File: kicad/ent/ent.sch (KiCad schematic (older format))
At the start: 28 parts, among them J1 Conn_01x04_Male, J2 Conn_01x03_Male, J3 Conn_01x03_Male, J4 Conn_01x12_Male, J5 Conn_01x04_Male, J6 Conn_01x03_Male, J7 Conn_01x03_Male, SW1 SW_SPDT, SW2 SW_Push, U1 TPS62172DSG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

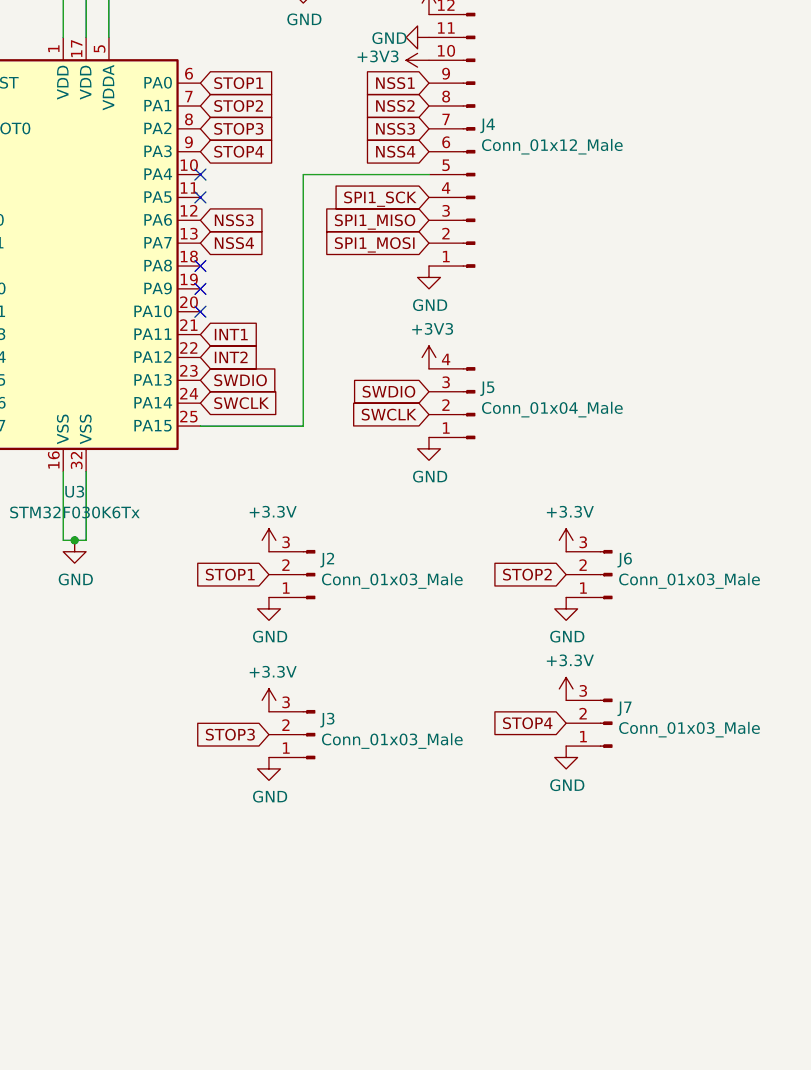
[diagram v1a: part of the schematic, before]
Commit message: added interface buttons
enkel schema
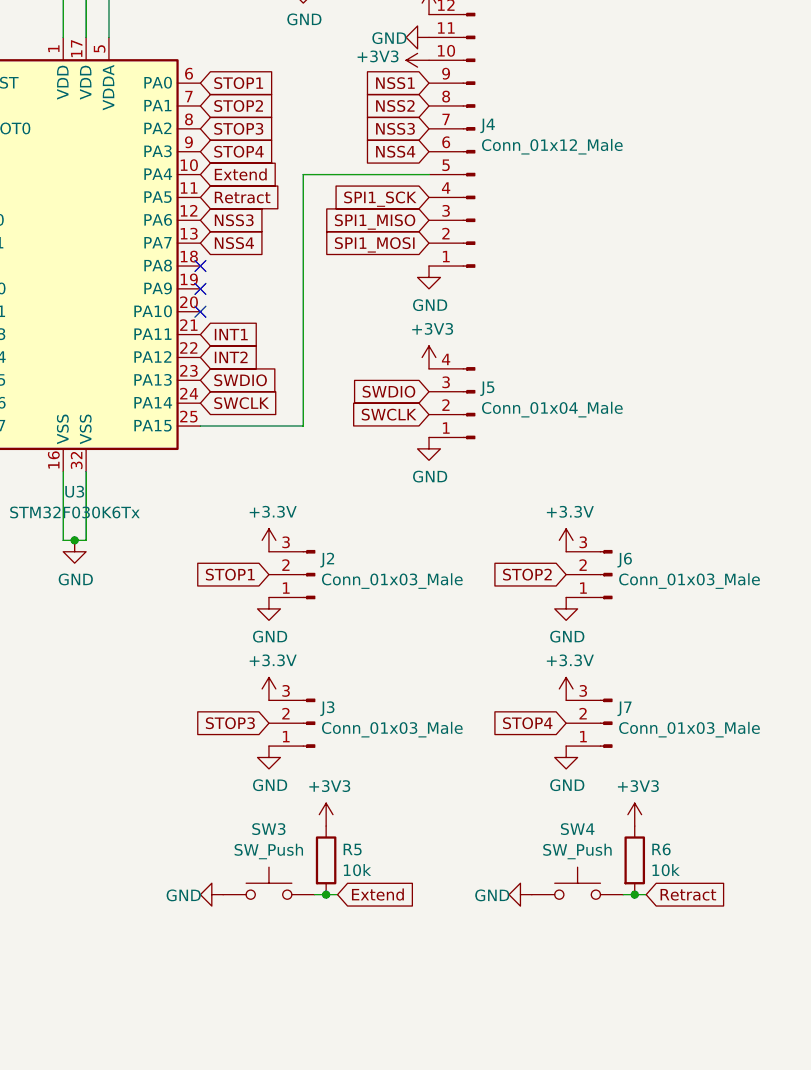
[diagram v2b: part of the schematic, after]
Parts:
- added R5, R6: 10k, Resistor_SMD:R_0805_2012Metric_Pad1.15x1.40mm_HandSolder, symbol Device:R
- added SW3, SW4: SW_Push, Button_Switch_SMD:SW_SPST_PTS645, symbol Switch:SW_Push
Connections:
- net +3V3: now also R5.1, R6.1
- net GND: now also SW3.1, SW4.1
- net Extend: now reaches U3.10 (PA4)
- net Extend: now also R5.2, SW3.2
- net Retract: now reaches U3.11 (PA5)
- net Retract: now also R6.2, SW4.2
- no-connect marks 7 -> 5
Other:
- moved on the sheet: J3
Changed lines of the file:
@@
 NoConn ~ 6700 2900
-$Comp
-L Switch:SW_Push SW2
-U 1 1 5E5EBC4B
-P 6300 2200
-F 0 "SW2" H 6300 2485 50  0000 C CNN
-F 1 "SW_Push" H 6300 2394 50  0000 C CNN
-F 2 "Button_Switch_SMD:SW_SPST_PTS645" H 6300 2400 50  0001 C CNN
-F 3 "~" H 6300 2400 50  0001 C CNN
-	1    6300 2200
-	1    0    0    -1
-$EndComp
-$Comp
-L power:GND #PWR014
-U 1 1 5E5EC8E1
-P 6100 2200
-F 0 "#PWR014" H 6100 1950 50  0001 C CNN
-F 1 "GND" V 6105 2027 50  0000 C CNN
-F 2 "" H 6100 2200 50  0001 C CNN
-F 3 "" H 6100 2200 50  0001 C CNN
-	1    6100 2200
-	0    1    1    0
-$EndComp
-Wire Wire Line
-	6500 2200 6600 2200
 $Comp
 L Device:C C5
@@
 	0    -1   -1   0
 $EndComp
-Wire Wire Line
-	6450 1800 6600 1800
-Wire Wire Line
-	6600 1800 6600 2200
-Connection ~ 6600 2200
-Wire Wire Line
-	6600 2200 6700 2200
 $Comp
 L power:GND #PWR015
@@
 Wire Wire Line
 	8250 2600 8800 2600
-NoConn ~ 7800 2600
-NoConn ~ 7800 2700
 Text GLabel 7800 2200 2    50   Input ~ 0
 STOP1
@@
 	1    0    0    -1
 $EndComp
-Text GLabel 8100 5050 0    50   Input ~ 0
+Text GLabel 8100 5000 0    50   Input ~ 0
 STOP3
 $Comp
 L Connector:Conn_01x03_Male J3
 U 1 1 5E66EF9D
-P 8300 5050
-F 0 "J3" H 8272 4982 50  0000 R CNN
-F 1 "Conn_01x03_Male" H 8272 5073 50  0000 R CNN
-F 2 "Connector_JST:JST_XH_B3B-XH-A_1x03_P2.50mm_Vertical" H 8300 5050 50  0001 C CNN
-F 3 "~" H 8300 5050 50  0001 C CNN
-	1    8300 5050
+P 8300 5000
+F 0 "J3" H 8272 4932 50  0000 R CNN
+F 1 "Conn_01x03_Male" H 8272 5023 50  0000 R CNN
+F 2 "Connector_JST:JST_XH_B3B-XH-A_1x03_P2.50mm_Vertical" H 8300 5000 50  0001 C CNN
+F 3 "~" H 8300 5000 50  0001 C CNN
+	1    8300 5000
 	-1   0    0    1
 $EndComp
@@
 L power:+3.3V #PWR023
 U 1 1 5E66EFA3
-P 8100 4950
-F 0 "#PWR023" H 8100 4800 50  0001 C CNN
-F 1 "+3.3V" H 8115 5123 50  0000 C CNN
-F 2 "" H 8100 4950 50  0001 C CNN
-F 3 "" H 8100 4950 50  0001 C CNN
-	1    8100 4950
+P 8100 4900
+F 0 "#PWR023" H 8100 4750 50  0001 C CNN
+F 1 "+3.3V" H 8115 5073 50  0000 C CNN
+F 2 "" H 8100 4900 50  0001 C CNN
+F 3 "" H 8100 4900 50  0001 C CNN
+	1    8100 4900
 	1    0    0    -1
 $EndComp
@@
 L power:GND #PWR024
 U 1 1 5E66EFA9
-P 8100 5150
-F 0 "#PWR024" H 8100 4900 50  0001 C CNN
-F 1 "GND" H 8105 4977 50  0000 C CNN
-F 2 "" H 8100 5150 50  0001 C CNN
-F 3 "" H 8100 5150 50  0001 C CNN
-	1    8100 5150
+P 8100 5100
+F 0 "#PWR024" H 8100 4850 50  0001 C CNN
+F 1 "GND" H 8105 4927 50  0000 C CNN
+F 2 "" H 8100 5100 50  0001 C CNN
+F 3 "" H 8100 5100 50  0001 C CNN
+	1    8100 5100
 	1    0    0    -1
 $EndComp
@@
 F1 "motor.sch" 50
 $EndSheet
+Text GLabel 7800 2700 2    50   Input ~ 0
+Retract
+Text GLabel 7800 2600 2    50   Input ~ 0
+Extend
+$Comp
+L power:GND #PWR014
+U 1 1 5E5EC8E1
+P 6100 2200
+F 0 "#PWR014" H 6100 1950 50  0001 C CNN
+F 1 "GND" V 6105 2027 50  0000 C CNN
+F 2 "" H 6100 2200 50  0001 C CNN
+F 3 "" H 6100 2200 50  0001 C CNN
+	1    6100 2200
+	0    1    1    0
+$EndComp
+$Comp
+L Switch:SW_Push SW2
+U 1 1 5E5EBC4B
+P 6300 2200
+F 0 "SW2" H 6300 2485 50  0000 C CNN
+F 1 "SW_Push" H 6300 2394 50  0000 C CNN
+F 2 "Button_Switch_SMD:SW_SPST_PTS645" H 6300 2400 50  0001 C CNN
+F 3 "~" H 6300 2400 50  0001 C CNN
+	1    6300 2200
+	1    0    0    -1
+$EndComp
+$Comp
+L power:GND #PWR070
+U 1 1 5E6E8B31
+P 7900 5750
+F 0 "#PWR070" H 7900 5500 50  0001 C CNN
+F 1 "GND" V 7905 5577 50  0000 C CNN
+F 2 "" H 7900 5750 50  0001 C CNN
+F 3 "" H 7900 5750 50  0001 C CNN
+	1    7900 5750
+	0    1    1    0
+$EndComp
+$Comp
+L Switch:SW_Push SW3
+U 1 1 5E6E8B37
+P 8100 5750
+F 0 "SW3" H 8100 6035 50  0000 C CNN
+F 1 "SW_Push" H 8100 5944 50  0000 C CNN
+F 2 "Button_Switch_SMD:SW_SPST_PTS645" H 8100 5950 50  0001 C CNN
+F 3 "~" H 8100 5950 50  0001 C CNN
+	1    8100 5750
+	1    0    0    -1
+$EndComp
+$Comp
+L power:GND #PWR072
+U 1 1 5E6ECA13
+P 9250 5750
+F 0 "#PWR072" H 9250 5500 50  0001 C CNN
+F 1 "GND" V 9255 5577 50  0000 C CNN
+F 2 "" H 9250 5750 50  0001 C CNN
+F 3 "" H 9250 5750 50  0001 C CNN
+	1    9250 5750
+	0    1    1    0
+$EndComp
+$Comp
+L Switch:SW_Push SW4
+U 1 1 5E6ECA19
+P 9450 5750
+F 0 "SW4" H 9450 6035 50  0000 C CNN
+F 1 "SW_Push" H 9450 5944 50  0000 C CNN
+F 2 "Button_Switch_SMD:SW_SPST_PTS645" H 9450 5950 50  0001 C CNN
+F 3 "~" H 9450 5950 50  0001 C CNN
+	1    9450 5750
+	1    0    0    -1
+$EndComp
+Text GLabel 8400 5750 2    50   Input ~ 0
+Extend
+Text GLabel 9750 5750 2    50   Input ~ 0
+Retract
+$Comp
+L Device:R R5
+U 1 1 5E6F2108
+P 8350 5600
+F 0 "R5" H 8420 5646 50  0000 L CNN
+F 1 "10k" H 8420 5555 50  0000 L CNN
+F 2 "Resistor_SMD:R_0805_2012Metric_Pad1.15x1.40mm_HandSolder" V 8280 5600 50  0001 C CNN
+F 3 "~" H 8350 5600 50  0001 C CNN
+	1    8350 5600
+	1    0    0    -1
+$EndComp
+$Comp
+L power:+3V3 #PWR071
+U 1 1 5E6F210E
+P 8350 5450
+F 0 "#PWR071" H 8350 5300 50  0001 C CNN
+F 1 "+3V3" H 8365 5623 50  0000 C CNN
+F 2 "" H 8350 5450 50  0001 C CNN
+F 3 "" H 8350 5450 50  0001 C CNN
+	1    8350 5450
+	1    0    0    -1
+$EndComp
+Wire Wire Line
+	8300 5750 8350 5750
+Connection ~ 8350 5750
+Wire Wire Line
+	8350 5750 8400 5750
+$Comp
+L Device:R R6
+U 1 1 5E6FBA5C
+P 9700 5600
+F 0 "R6" H 9770 5646 50  0000 L CNN
+F 1 "10k" H 9770 5555 50  0000 L CNN
+F 2 "Resistor_SMD:R_0805_2012Metric_Pad1.15x1.40mm_HandSolder" V 9630 5600 50  0001 C CNN
+F 3 "~" H 9700 5600 50  0001 C CNN
+	1    9700 5600
+	1    0    0    -1
+$EndComp
+$Comp
+L power:+3V3 #PWR073
+U 1 1 5E6FBA62
+P 9700 5450
+F 0 "#PWR073" H 9700 5300 50  0001 C CNN
+F 1 "+3V3" H 9715 5623 50  0000 C CNN
+F 2 "" H 9700 5450 50  0001 C CNN
+F 3 "" H 9700 5450 50  0001 C CNN
+	1    9700 5450
+	1    0    0    -1
+$EndComp
+Wire Wire Line
+	9650 5750 9700 5750
+Connection ~ 9700 5750
+Wire Wire Line
+	9700 5750 9750 5750
+Connection ~ 6600 2200
+Wire Wire Line
+	6500 2200 6600 2200
+Wire Wire Line
+	6600 2200 6700 2200
+Wire Wire Line
+	6600 1800 6600 2200
+Wire Wire Line
+	6450 1800 6600 1800
 $EndSCHEMATC

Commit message: pcb's
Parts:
- SW3, SW4: footprint Button_Switch_SMD:SW_SPST_PTS645 -> Connector_JST:JST_XH_B2B-XH-A_1x02_P2.50mm_Vertical
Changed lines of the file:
@@
 F 0 "SW3" H 8100 6035 50  0000 C CNN
 F 1 "SW_Push" H 8100 5944 50  0000 C CNN
-F 2 "Button_Switch_SMD:SW_SPST_PTS645" H 8100 5950 50  0001 C CNN
+F 2 "Connector_JST:JST_XH_B2B-XH-A_1x02_P2.50mm_Vertical" H 8100 5950 50  0001 C CNN
 F 3 "~" H 8100 5950 50  0001 C CNN
 	1    8100 5750
@@
 F 0 "SW4" H 9450 6035 50  0000 C CNN
 F 1 "SW_Push" H 9450 5944 50  0000 C CNN
-F 2 "Button_Switch_SMD:SW_SPST_PTS645" H 9450 5950 50  0001 C CNN
+F 2 "Connector_JST:JST_XH_B2B-XH-A_1x02_P2.50mm_Vertical" H 9450 5950 50  0001 C CNN
 F 3 "~" H 9450 5950 50  0001 C CNN
 	1    9450 5750

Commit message: pcb done
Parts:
- added D2: LED, LED_SMD:LED_0805_2012Metric_Pad1.15x1.40mm_HandSolder, symbol Device:LED
- added H1, H2, H3, H4: MountingHole_Pad, MountingHole:MountingHole_2.2mm_M2_Pad, symbol Mechanical:MountingHole_Pad
- added R7: R_Small, Resistor_SMD:R_0805_2012Metric_Pad1.15x1.40mm_HandSolder, symbol Device:R_Small
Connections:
- net GND: now also D2.1 (K), H1.1, H2.1, H3.1, H4.1
- net LED: now reaches U3.20 (PA10)
- net LED: now also R7.2
- new net: D2.2 (A), R7.1
- no-connect marks 5 -> 4
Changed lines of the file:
@@
 NoConn ~ 7800 3000
 NoConn ~ 7800 3100
-NoConn ~ 7800 3200
 NoConn ~ 6700 2800
 NoConn ~ 6700 2900
@@
 Wire Wire Line
 	6450 1800 6600 1800
+$Comp
+L Mechanical:MountingHole_Pad H3
+U 1 1 5E70361A
+P 2250 800
+F 0 "H3" H 2350 849 50  0000 L CNN
+F 1 "MountingHole_Pad" H 2350 758 50  0000 L CNN
+F 2 "MountingHole:MountingHole_2.2mm_M2_Pad" H 2250 800 50  0001 C CNN
+F 3 "~" H 2250 800 50  0001 C CNN
+	1    2250 800
+	1    0    0    -1
+$EndComp
+$Comp
+L Mechanical:MountingHole_Pad H4
+U 1 1 5E70514A
+P 2250 1250
+F 0 "H4" H 2350 1299 50  0000 L CNN
+F 1 "MountingHole_Pad" H 2350 1208 50  0000 L CNN
+F 2 "MountingHole:MountingHole_2.2mm_M2_Pad" H 2250 1250 50  0001 C CNN
+F 3 "~" H 2250 1250 50  0001 C CNN
+	1    2250 1250
+	1    0    0    -1
+$EndComp
+$Comp
+L Mechanical:MountingHole_Pad H1
+U 1 1 5E708109
+P 1350 800
+F 0 "H1" H 1450 849 50  0000 L CNN
+F 1 "MountingHole_Pad" H 1450 758 50  0000 L CNN
+F 2 "MountingHole:MountingHole_2.2mm_M2_Pad" H 1350 800 50  0001 C CNN
+F 3 "~" H 1350 800 50  0001 C CNN
+	1    1350 800
+	1    0    0    -1
+$EndComp
+$Comp
+L Mechanical:MountingHole_Pad H2
+U 1 1 5E70B210
+P 1350 1250
+F 0 "H2" H 1450 1299 50  0000 L CNN
+F 1 "MountingHole_Pad" H 1450 1208 50  0000 L CNN
+F 2 "MountingHole:MountingHole_2.2mm_M2_Pad" H 1350 1250 50  0001 C CNN
+F 3 "~" H 1350 1250 50  0001 C CNN
+	1    1350 1250
+	1    0    0    -1
+$EndComp
+$Comp
+L power:GND #PWR0101
+U 1 1 5E713E17
+P 2250 900
+F 0 "#PWR0101" H 2250 650 50  0001 C CNN
+F 1 "GND" H 2255 727 50  0000 C CNN
+F 2 "" H 2250 900 50  0001 C CNN
+F 3 "" H 2250 900 50  0001 C CNN
+	1    2250 900
+	1    0    0    -1
+$EndComp
+$Comp
+L power:GND #PWR0102
+U 1 1 5E7153B7
+P 2250 1350
+F 0 "#PWR0102" H 2250 1100 50  0001 C CNN
+F 1 "GND" H 2255 1177 50  0000 C CNN
+F 2 "" H 2250 1350 50  0001 C CNN
+F 3 "" H 2250 1350 50  0001 C CNN
+	1    2250 1350
+	1    0    0    -1
+$EndComp
+$Comp
+L power:GND #PWR0103
+U 1 1 5E71835A
+P 1350 1350
+F 0 "#PWR0103" H 1350 1100 50  0001 C CNN
+F 1 "GND" H 1355 1177 50  0000 C CNN
+F 2 "" H 1350 1350 50  0001 C CNN
+F 3 "" H 1350 1350 50  0001 C CNN
+	1    1350 1350
+	1    0    0    -1
+$EndComp
+$Comp
+L power:GND #PWR0104
+U 1 1 5E71B389
+P 1350 900
+F 0 "#PWR0104" H 1350 650 50  0001 C CNN
+F 1 "GND" H 1355 727 50  0000 C CNN
+F 2 "" H 1350 900 50  0001 C CNN
+F 3 "" H 1350 900 50  0001 C CNN
+	1    1350 900
+	1    0    0    -1
+$EndComp
+Text GLabel 7800 3200 2    50   Input ~ 0
+LED
+Text GLabel 6650 4800 0    50   Input ~ 0
+LED
+$Comp
+L Device:LED D2
+U 1 1 5E727196
+P 7150 4800
+F 0 "D2" H 7143 4545 50  0000 C CNN
+F 1 "LED" H 7143 4636 50  0000 C CNN
+F 2 "LED_SMD:LED_0805_2012Metric_Pad1.15x1.40mm_HandSolder" H 7150 4800 50  0001 C CNN
+F 3 "~" H 7150 4800 50  0001 C CNN
+	1    7150 4800
+	-1   0    0    1
+$EndComp
+$Comp
+L Device:R_Small R7
+U 1 1 5E72864D
+P 6900 4800
+F 0 "R7" V 6704 4800 50  0000 C CNN
+F 1 "R_Small" V 6795 4800 50  0000 C CNN
+F 2 "Resistor_SMD:R_0805_2012Metric_Pad1.15x1.40mm_HandSolder" H 6900 4800 50  0001 C CNN
+F 3 "~" H 6900 4800 50  0001 C CNN
+	1    6900 4800
+	0    1    1    0
+$EndComp
+Wire Wire Line
+	6650 4800 6800 4800
+$Comp
+L power:GND #PWR0105
+U 1 1 5E732DB4
+P 7450 4850
+F 0 "#PWR0105" H 7450 4600 50  0001 C CNN
+F 1 "GND" H 7455 4677 50  0000 C CNN
+F 2 "" H 7450 4850 50  0001 C CNN
+F 3 "" H 7450 4850 50  0001 C CNN
+	1    7450 4850
+	1    0    0    -1
+$EndComp
+Wire Wire Line
+	7300 4800 7450 4800
+Wire Wire Line
+	7450 4800 7450 4850
 $EndSCHEMATC
